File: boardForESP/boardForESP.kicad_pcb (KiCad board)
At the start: 2 copper layers, 73.7 x 53.3 mm, 6 parts, among them J1 Conn_01x15_Socket, J2 Conn_01x15_Socket

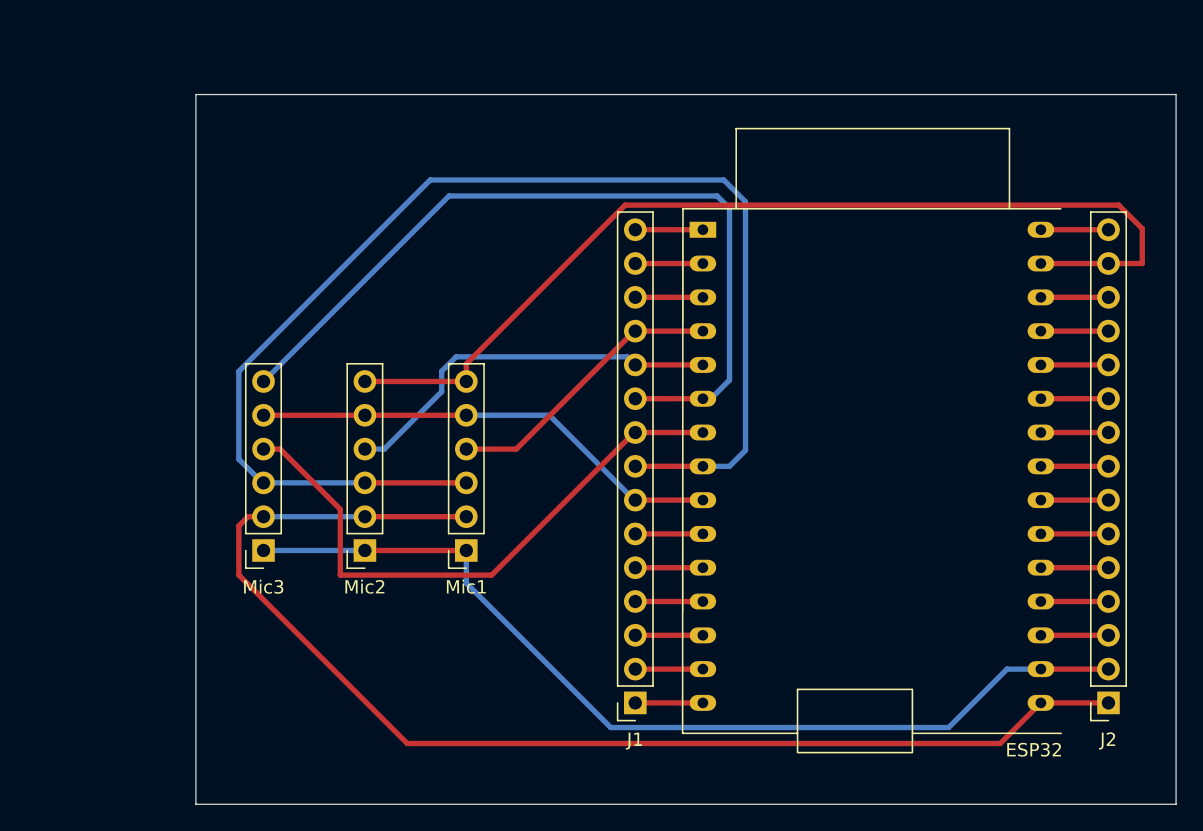
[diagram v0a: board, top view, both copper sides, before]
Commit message: Refactor junctions and wires in the schematic for improved connectivity and layout. Added new junctions at specified coordinates and updated wire connections accordingly. Removed redundant junction and adjusted UUIDs for consistency. Created a lock file for PCB design to prevent concurrent modifications.
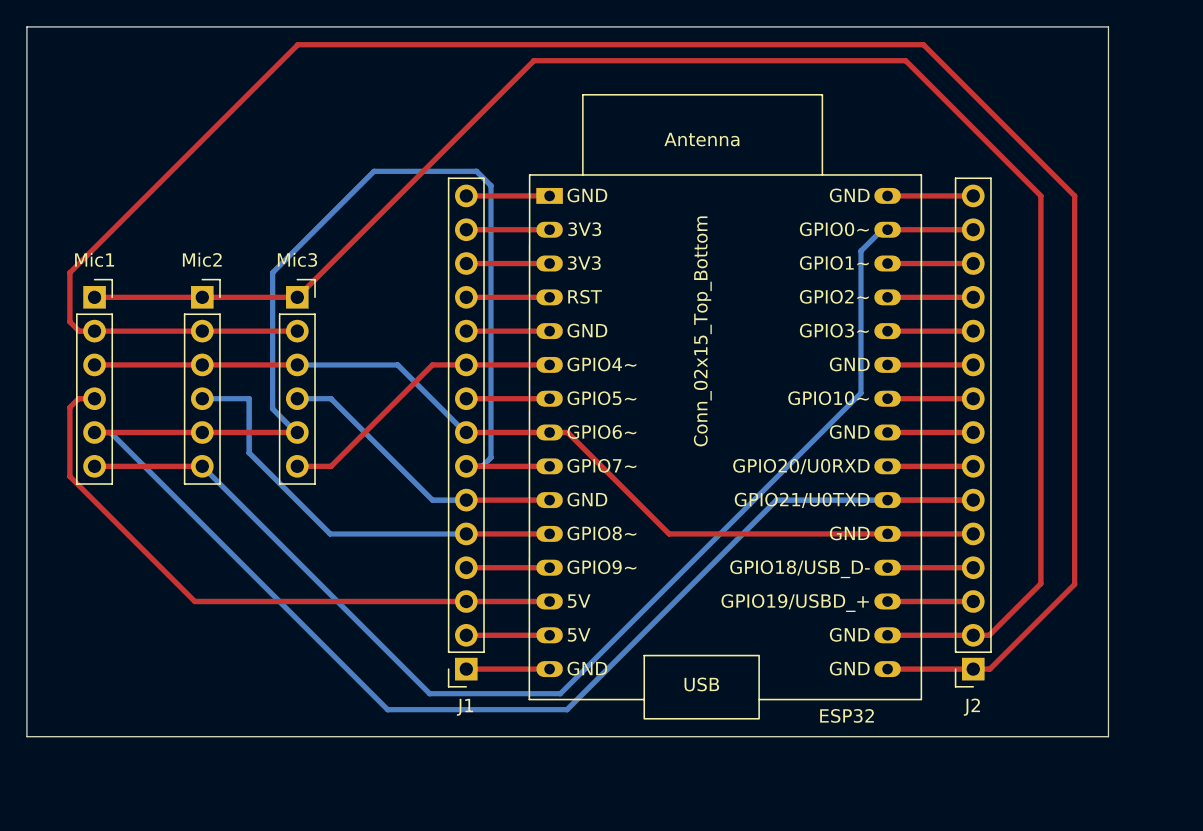
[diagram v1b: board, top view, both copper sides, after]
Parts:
- moved Mic1 33.8 mm to (76.2, 76.2), turned to 0 degrees
- moved Mic2 22.6 mm to (84.3, 76.2), turned to 0 degrees
- moved Mic3 19.2 mm to (91.4, 76.2), turned to 0 degrees
- moved J1 13.0 mm to (104.1, 104.1)
- moved ESP32 11.8 mm to (110.4, 68.6)
- moved J2 10.5 mm to (142.2, 104.1)
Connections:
- ESP32 pad 26: Net-(ESP32-GPIO4) -> Net-(ESP32-GPIO25)
- ESP32 pad 9: Net-(ESP32-GPIO26) -> Net-(ESP32-GPIO16)
- J1 pad 7: Net-(ESP32-GPIO26) -> Net-(ESP32-GPIO16)
- J2 pad 5: Net-(ESP32-GPIO4) -> Net-(ESP32-GPIO25)
- Mic1 pad 4: Net-(ESP32-GPIO34) -> Net-(ESP32-GPIO13)
- Mic1 pad 5: Net-(ESP32-GPIO26) -> Net-(ESP32-GPIO16)
- Mic2 pad 4: Net-(ESP32-GPIO35) -> Net-(ESP32-GPIO14)
- Mic2 pad 5: Net-(ESP32-GPIO26) -> Net-(ESP32-GPIO16)
- Mic3 pad 4: Net-(ESP32-GPIO33) -> Net-(ESP32-GPIO27)
- Mic3 pad 5: Net-(ESP32-GPIO26) -> Net-(ESP32-GPIO16)
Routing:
- net Net-(ESP32-GPIO16): track 5.08 -> 164.5 mm
- net +3V3: track 92.9 -> 154.3 mm
- net GND: track 72.3 -> 125.0 mm
- net Net-(ESP32-GPIO13): track 5.08 -> 47.3 mm
- net Net-(ESP32-GPIO32): track 61.7 -> 22.1 mm
- net Net-(ESP32-GPIO33): track 44.4 -> 6.26 mm
- net Net-(ESP32-GPIO26): track 35.7 -> 0.00 mm
- net Net-(ESP32-GPIO14): track 5.08 -> 32.7 mm
- net Net-(ESP32-GPIO25): track 96.6 -> 71.3 mm
- net Net-(ESP32-GPIO35): track 29.4 -> 6.26 mm
- net Net-(ESP32-GPIO22): track 75.7 -> 93.8 mm
- net Net-(ESP32-GPIO27): track 5.08 -> 22.1 mm
- net Net-(ESP32-GPIO34): track 21.5 -> 6.26 mm
- net Net-(ESP32-GPIO4): track 5.08 -> 0.00 mm
- net Net-(ESP32-GPIO5): track 5.08 -> 6.44 mm
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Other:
- board size 73.7 x 53.3 mm -> 81.3 x 53.3 mm
- board text removed: "Antenna"
- board text removed: "USB"
